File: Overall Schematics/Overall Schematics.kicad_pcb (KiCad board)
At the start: 2 copper layers, 152.4 x 167.9 mm, 33 parts, among them J1 WattMeter1_Output, J2 WattMeter2_Output, J3 Intel_Buck_Converter_Input, M1 Stepper_Motor_bipolar, M10 Motor_Servo, M11 Stepper_Motor_bipolar, M12 Motor_Servo, M2 Stepper_Motor_bipolar, M3 LinActuator12V, M4 LinActuator12V, M5 LinActuator12V, M6 Motor_DC, M7 Motor_DC, M8 Motor_DC, M9 Motor_DC, U1 Teensy4.1, U10 VNH52019, U11 ServoDriver, U12 36v4SMD, U13 D24V22F5, U2 36v4SMD, U3 36v4SMD, U4 VNH52019, U5 VNH52019, U6 VNH52019, U7 VNH52019, U8 VNH52019, U9 VNH52019

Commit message: added small adjustments
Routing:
- net AOUT1_3: track 12.3 -> 14.8 mm
- net BOUT2_3: track 9.06 -> 9.69 mm

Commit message: Beginning Design fixes
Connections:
- U10 pad 11: OUTA_4 -> Battery1_Positive24V
- U10 pad 12: OUTB_4 -> PWR_GND
- U10 pad 13: PWR_GND -> OUTB_2
- U10 pad 14: Battery1_Positive24V -> OUTA_1
- U4 pad 11: OUTA2_LIN -> Battery1_Positive24V
- U4 pad 12: OUTB2_LIN -> PWR_GND
- U4 pad 13: PWR_GND -> OUTB2_LIN
- U4 pad 14: Battery1_Positive24V -> OUTA2_LIN
- U7 pad 11: OUTA_1 -> Battery1_Positive24V
- U7 pad 12: OUTB_1 -> PWR_GND
- U7 pad 13: PWR_GND -> OUTB_1
- U7 pad 14: Battery1_Positive24V -> OUTA_1
- U8 pad 11: OUTA_2 -> Battery1_Positive24V
- U8 pad 12: OUTB_2 -> PWR_GND
- U8 pad 13: PWR_GND -> OUTB_2
- U8 pad 14: Battery1_Positive24V -> OUTA_2
- U9 pad 11: OUTA_3 -> Battery1_Positive24V
- U9 pad 12: OUTB_3 -> PWR_GND
- U9 pad 14: Battery1_Positive24V -> OUTA_3
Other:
- net class 3.3V removed
- net class Default removed
- net class Power removed
- net class Signal removed

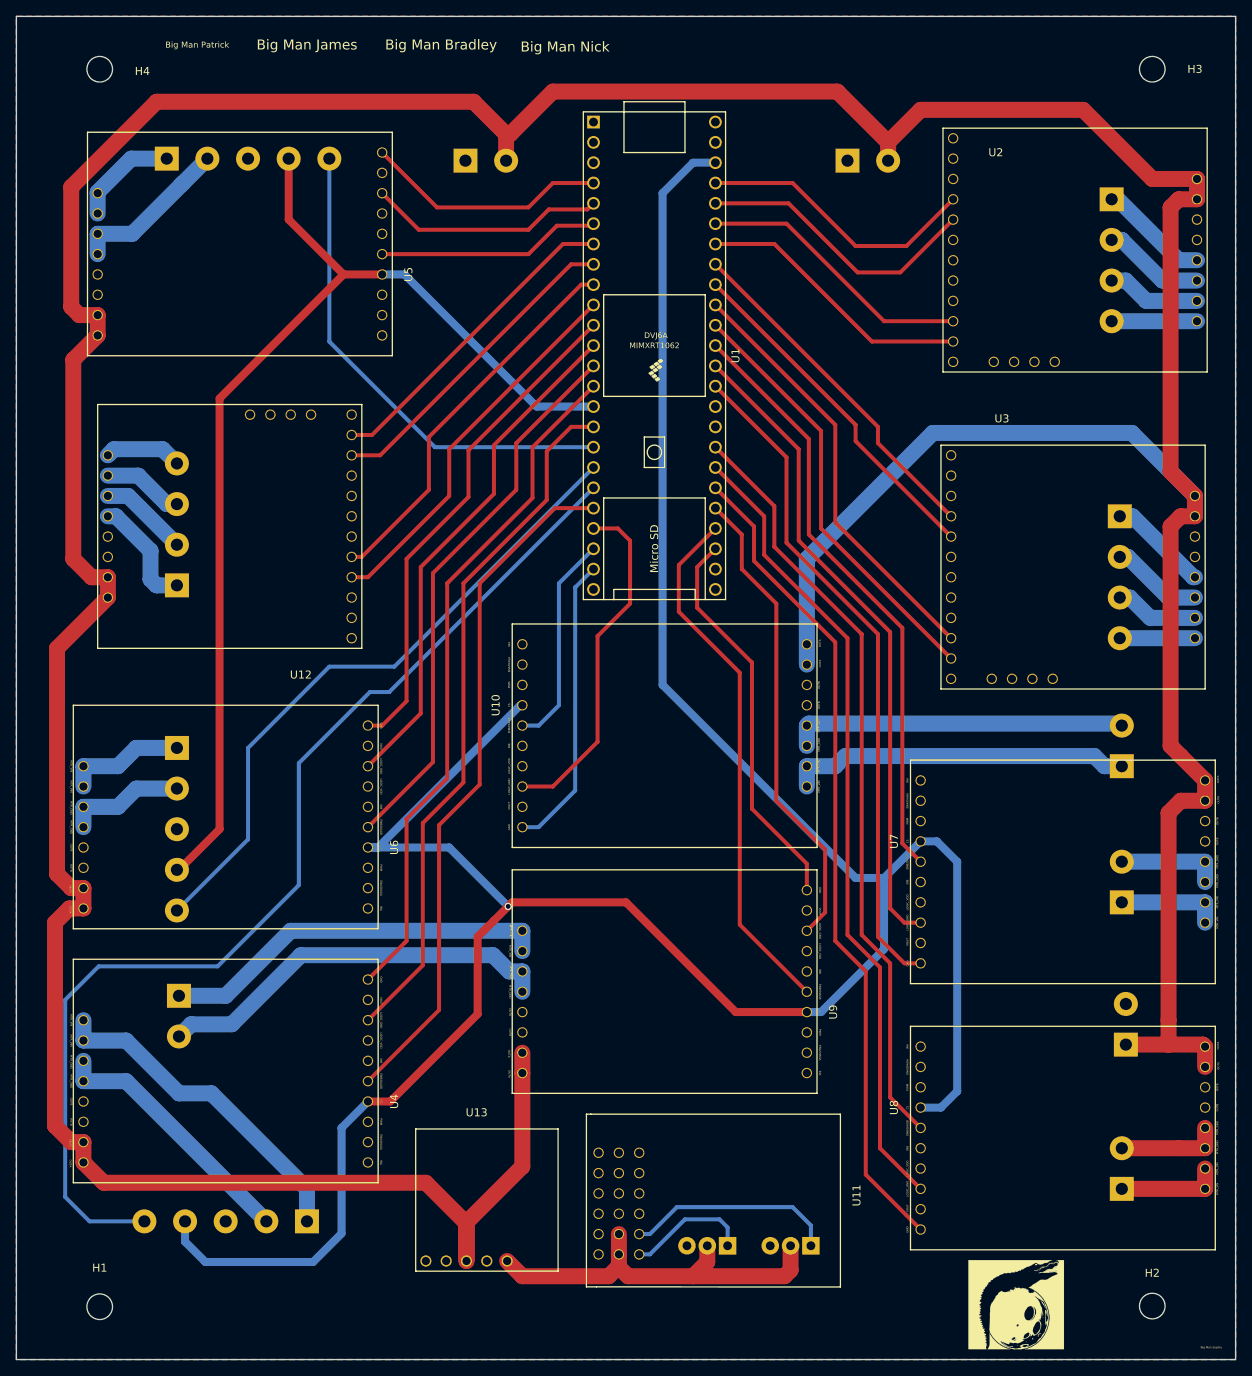
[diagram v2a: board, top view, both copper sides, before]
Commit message: Changing VNH5019 layout to match physical
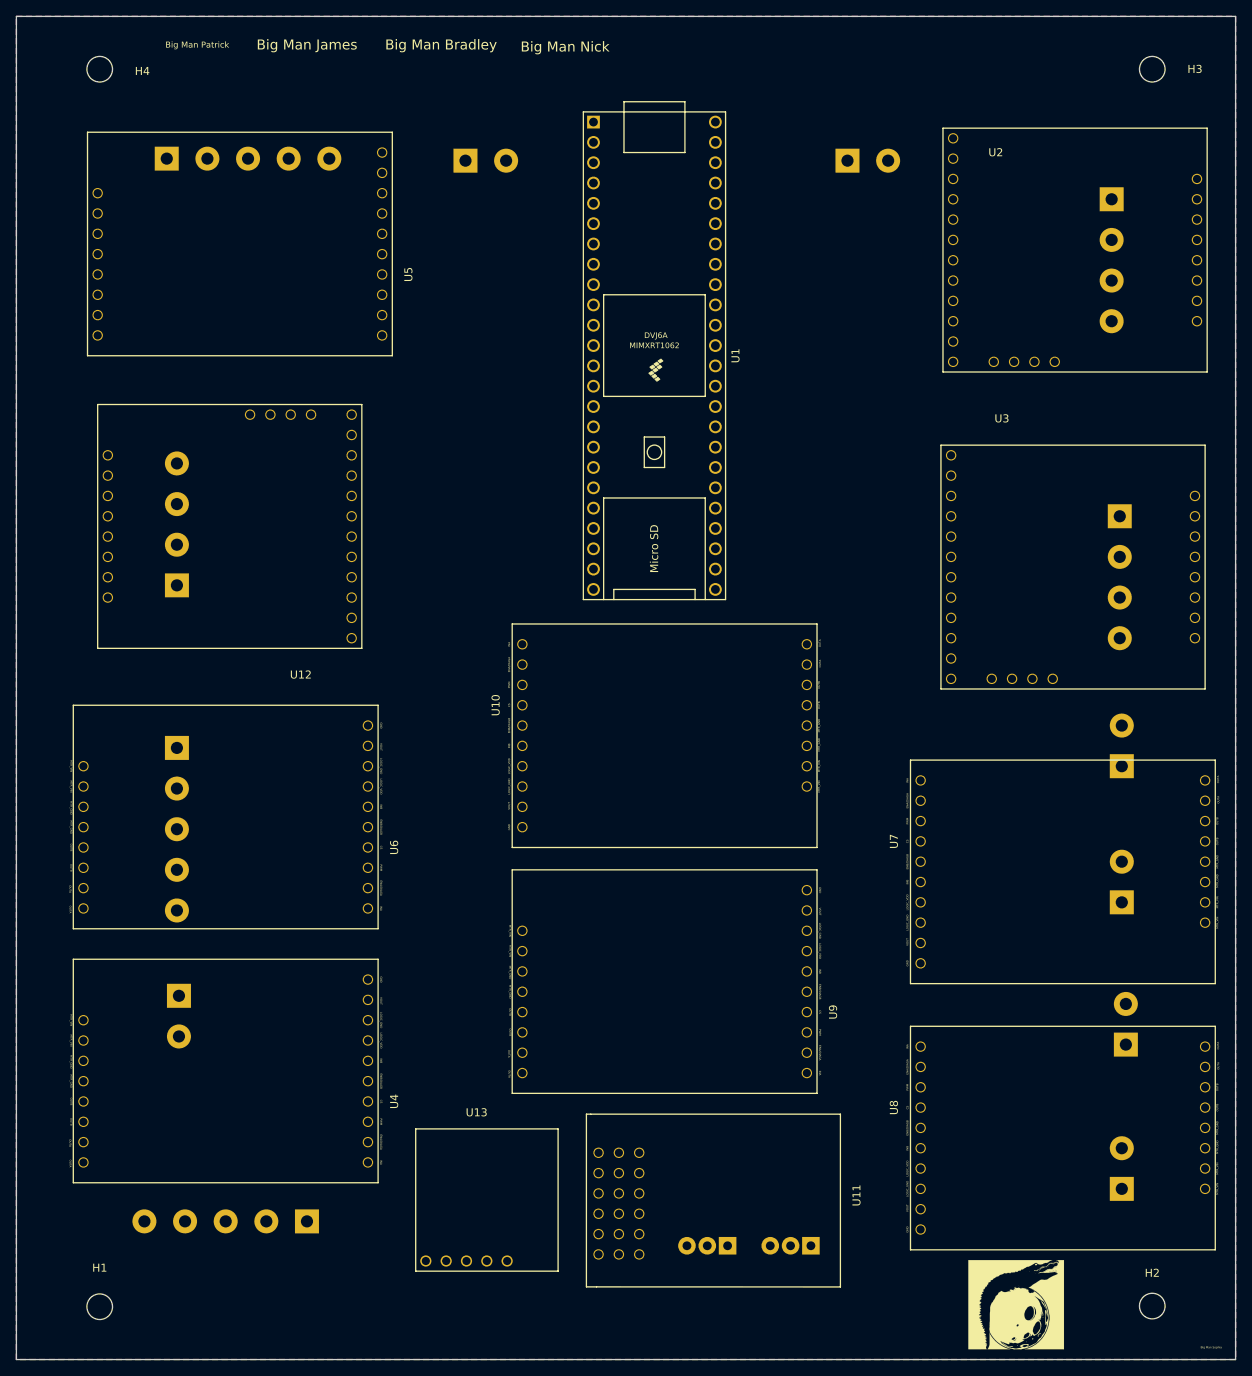
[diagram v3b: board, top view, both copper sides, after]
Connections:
- U9 pad 11: Battery1_Positive24V -> OUTA_3
- U9 pad 12: PWR_GND -> OUTB_3
- U9 pad 14: OUTA_3 -> Battery1_Positive24V
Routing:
- net Battery1_Positive24V: track 589.8 -> 0.00 mm
- net 3.3V: track 480.3 -> 0.00 mm, vias 1 -> 0
- net LIN_SIGNAL2: track 137.3 -> 0.00 mm
- net INA_2: track 103.3 -> 0.00 mm
- net PWM_2: track 100.8 -> 0.00 mm
- net INB_2: track 95.7 -> 0.00 mm
- net PWM_6: track 87.5 -> 0.00 mm
- net INB_6: track 86.1 -> 0.00 mm
- net INA_6: track 85.8 -> 0.00 mm
- net INA_1: track 84.0 -> 0.00 mm
- net LIN_SIGNAL1: track 81.7 -> 0.00 mm
- net PWM_1: track 81.4 -> 0.00 mm
- net INB_1: track 75.1 -> 0.00 mm
- net INB_5: track 69.3 -> 0.00 mm
- net INB_3: track 66.4 -> 0.00 mm
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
